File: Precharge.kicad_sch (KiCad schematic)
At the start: 11 parts, among them J1 MicroFit+, J2 JST-XA, K1 DAR71205, Q1 BSS205N, U1 NCP1117

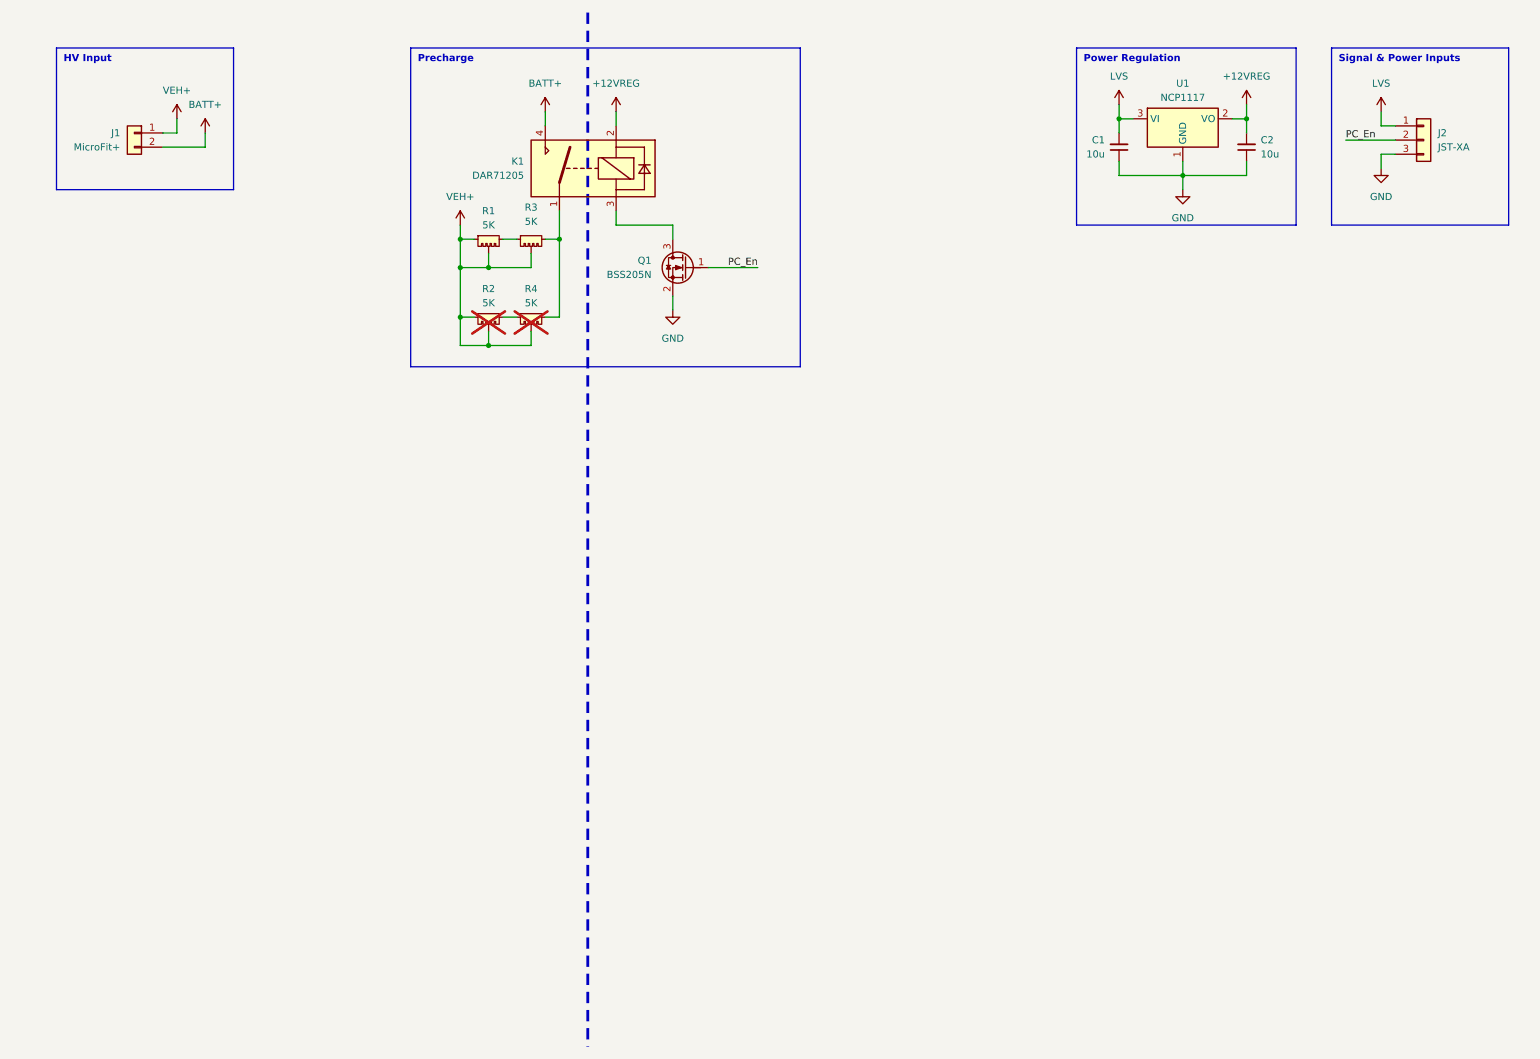
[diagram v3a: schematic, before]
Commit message: TSAL compatibility, shortened precharge, simpler LV
Back to 4 resistors, so short precharge time, and powering relay from BMS GPIO. Cut SCS and regulation. added TSAL circuitry to allow for relay state measurement with single contact.
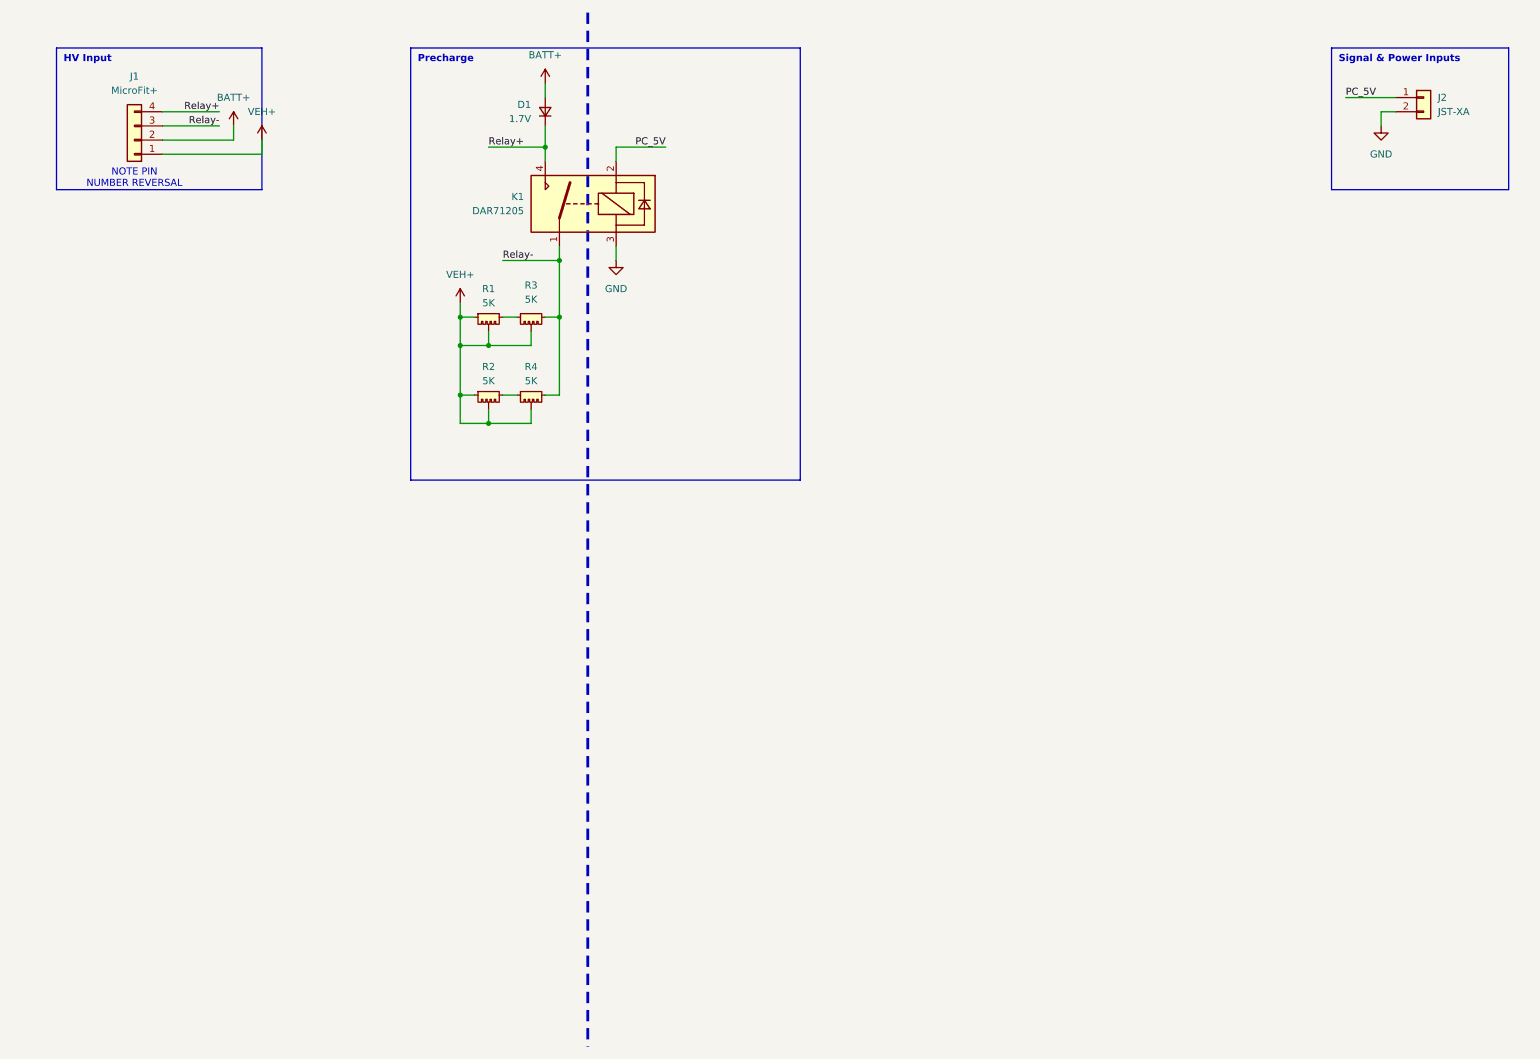
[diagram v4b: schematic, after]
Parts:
- removed C1, C2: 10u, Library:C_1206_3216Metric_Pad1.33x1.80mm_HandSolder, symbol Device:C_Small
- removed J1: MicroFit+, Library:Connector_MicroFit-Plus_2POS, symbol Custom_MSM.old:Connector_MicroFit-Plus_2POS
- removed J2: JST-XA, Library:Connector_JST-XA_3POS, symbol Custom_MSM:Connector_JST-XA_3POS
- removed Q1: BSS205N, Library:MOSFET_Single_SOT-23, symbol Custom_MSM:MOSFET_N-CH
- removed U1: NCP1117, Library:Regulator_Linear_SOT-223-4, symbol Custom_MSM:Regulator_Linear_12V
- added D1: 1.7V, Diode_SMD:D_SOD-123F, symbol Device:D_Small
- added J1: MicroFit+, Custom_MSM:Connector_MicroFit-Plus_4POS, symbol Custom_MSM:Connector_MicroFit-Plus_4POS
- added J2: JST-XA, Custom_MSM:Connector_JST-XA_2POS, symbol Custom_MSM:Connector_JST-XA_2POS
- R2, R4: now fitted
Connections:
- net BATT+: now also D1.2 (A), J1.2 (Pin_2); no longer K1.4
- net GND: now also K1.3, J2.2 (Pin_2)
- net VEH+: now also J1.1 (Pin_1)
- net Relay-: now reaches K1.1, R3.3, R4.3
- net Relay-: now also J1.3 (Pin_3)
- net +12VREG renamed PC_5V
- net PC_5V: now also J2.1 (Pin_1)
- new net Relay+: D1.1 (K), J1.4 (Pin_4), K1.4
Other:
- note added: "NOTE PIN NUMBER REVERSAL"
- note removed: "Power Regulation"
- moved on the sheet: K1, R1, R3
